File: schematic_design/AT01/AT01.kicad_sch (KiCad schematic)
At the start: 58 parts, among them J1 JST Connector, J2 Conn_01x08, J3 USB_C_Receptacle_USB2.0, J4 DC Pump Connector, J5 Solenoid Valve Connector, Q1 DMG2301L, Q2 2N7002, Q3 2N7002, SW1 SW_Push, SW2 SW_Push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

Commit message: added redesigned charging circuit
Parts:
- removed D2: LED, LED_THT:LED_D3.0mm, symbol Device:LED
- removed U4: MCP73831-2-OT, Package_TO_SOT_SMD:SOT-23-5, symbol Battery_Management:MCP73831-2-OT
- added C12, C9: 10uF, Capacitor_SMD:C_0603_1608Metric_Pad1.08x0.95mm_HandSolder, symbol Device:C
- added C15: 0.1uF, Capacitor_SMD:C_0603_1608Metric_Pad1.08x0.95mm_HandSolder, symbol Device:C_Small
- added C16: 10uF, Capacitor_SMD:C_0603_1608Metric_Pad1.08x0.95mm_HandSolder, symbol Device:C_Small
- added D10: LED, LED_THT:LED_D3.0mm, symbol Device:LED
- added D2, D9: MBRM120LT3G, Diode_SMD:D_SOD-123F, symbol Diode:MBR1020VL
- added L1: 2.7u, symbol Device:L
- added Q4: FDS6375, FDS6375:SOIC127P600X175-8N, symbol FDS6375:FDS6375
- added R18: 100m, Resistor_SMD:R_0603_1608Metric_Pad0.98x0.95mm_HandSolder, symbol Device:R
- added R19: 100K, Resistor_SMD:R_0603_1608Metric_Pad0.98x0.95mm_HandSolder, symbol Device:R
- added U4: LT1935ES5-TRPBF, S_5_ADI, symbol 2023-10-27_15-39-09:LT1935ES5-TRPBF
- added U7: MCP73844T-840I/MS, MSOP8_MC_MCH, symbol 2023-10-27_15-39-09:MCP73844T-840I_MS
- C14: footprint Capacitor_SMD:C_0402_1005Metric_Pad0.74x0.62mm_HandSolder -> CAP_FN_C_PAN; symbol Device:C_Small -> 2023-10-27_15-39-09:EEE-FN1A101UR
- C7: footprint Capacitor_SMD:C_0402_1005Metric_Pad0.74x0.62mm_HandSolder -> Capacitor_SMD:C_0603_1608Metric_Pad1.08x0.95mm_HandSolder
- J4, J5: footprint Connector_JST:JST_EH_S2B-EH_1x02_P2.50mm_Horizontal -> TerminalBlock_4Ucon:TerminalBlock_4Ucon_1x02_P3.50mm_Vertical
- R10: value 5.1K -> 10K; footprint Resistor_SMD:R_0402_1005Metric_Pad0.72x0.64mm_HandSolder -> Resistor_SMD:R_0603_1608Metric_Pad0.98x0.95mm_HandSolder
- R9: value 5.1K -> 61.2K
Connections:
- net GND: now also C14.1, C7.2, R10.2, C12.2, C15.2, C16.2, C9.2, U4.2 (GND), U7.6 (VSS); no longer C14.2, C7.1, R9.2
- net VBAT: now also C14.2, C16.1, Q4.5, U7.7 (VBAT); no longer C14.1, C7.2
- net VBUS: now also C7.1, L1.1, U4.4 (*SHDN), U4.5 (VIN)
- net at R10.1: now also R9.2, U4.3 (FB)
- net at R9.1: now also C9.1, D2.1 (K), D9.2 (A)
- new net: C15.1, U7.5 (TIMER)
- new net: Q4.1, R18.2, U7.1 (SENSE)
- new net: Q4.4, U7.8 (DRV)
- new net: C12.1, D10.2 (A), D9.1 (K), R18.1, R19.1, U7.2 (VDD)
- new net: D10.1 (K), U7.3 (STAT1)
- new net: R19.2, U7.4 (EN)
- new net: D2.2 (A), L1.2, U4.1 (SW)
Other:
- added sheet AT01_Lipo (AT01_Lipo.kicad_sch)
- note added: "9V"
- moved on the sheet: C10, C13, C8, D1, H1, H2, H3, H4, J1, Q1, R3, U6

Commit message: updated FTDI board
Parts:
- removed J2: Conn_01x08, Connector_PinHeader_1.00mm:PinHeader_1x08_P1.00mm_Vertical, symbol Connector_Generic:Conn_01x08
- added C17: 0.1uF, Capacitor_SMD:C_0402_1005Metric_Pad0.74x0.62mm_HandSolder, symbol Device:C
- added C18: 10uF, Capacitor_SMD:C_0402_1005Metric_Pad0.74x0.62mm_HandSolder, symbol Device:C_Small
- added J2: Conn_01x07, Connector_PinHeader_1.00mm:PinHeader_1x07_P1.00mm_Vertical, symbol Connector_Generic:Conn_01x07
- added R20: 5.1K, Resistor_SMD:R_0402_1005Metric_Pad0.72x0.64mm_HandSolder, symbol Device:R
- C12, C15, C16, C7, C9: footprint Capacitor_SMD:C_0603_1608Metric_Pad1.08x0.95mm_HandSolder -> Capacitor_SMD:C_0402_1005Metric_Pad0.74x0.62mm_HandSolder
- J4, J5: footprint TerminalBlock_4Ucon:TerminalBlock_4Ucon_1x02_P3.50mm_Vertical -> TerminalBlock_4Ucon:TerminalBlock_4Ucon_1x02_P3.50mm_Horizontal
- L1: footprint (none) -> Library:IND_R2NC_SUM
- Q4: footprint FDS6375:SOIC127P600X175-8N -> Library:SOIC127P600X175-8N
- R10, R18, R19: footprint Resistor_SMD:R_0603_1608Metric_Pad0.98x0.95mm_HandSolder -> Capacitor_SMD:C_0402_1005Metric_Pad0.74x0.62mm_HandSolder
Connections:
- net BL_SCREEN is gone; now on net SDA: U5.7 (IO35)
- net 3V3: now also C17.1, J2.1 (Pin_1), R20.1
- net CS: now also U5.14 (IO12), J2.6 (Pin_6); no longer U5.8 (IO32)
- net DC_SCREEN: now also U5.10 (IO25), J2.3 (Pin_3); no longer U5.9 (IO33)
- net DRV_FAULT: now also U5.26 (IO4); no longer U5.12 (IO27)
- net DRV_SLEEP: now also U5.27 (IO16); no longer U5.11 (IO26)
- net GND: now also C17.2, C18.2, J2.2 (Pin_2)
- net GPIO0: now also R20.2
- net MOSI: now also U5.16 (IO13), J2.7 (Pin_7); no longer U5.30 (IO18)
- net MOTOR_PIN_1: now also U5.30 (IO18); no longer U5.14 (IO12)
- net MOTOR_PIN_2: now also U5.31 (IO19); no longer U5.16 (IO13)
- net RST_SCREEN: now also U5.11 (IO26), J2.4 (Pin_4); no longer U5.6 (IO34)
- net SCK: now also U5.13 (IO14), J2.5 (Pin_5); no longer U5.29 (IO5)
- net SCL: now also U5.6 (IO34); no longer U5.36 (IO22)
- net SDA: no longer U5.37 (IO23)
- net SOLENOID_PIN_1: now also U5.28 (IO17); no longer U5.13 (IO14)
- net SOLENOID_PIN_2: now also U5.29 (IO5); no longer U5.23 (IO15)
- net VBAT: now also Q1.2 (S); no longer Q1.3 (D)
- net at R17.2, SW3.2: now also U5.36 (IO22); no longer U5.10 (IO25)
- net at R15.2: now also U5.23 (IO15); no longer U5.27 (IO16)
- net at R16.2, SW2.2: now also U5.37 (IO23); no longer U5.33 (IO21)
- net at R11.2, R8.1, U5.4 (SENSOR_VP): now also C18.1
- net at C8.1, D1.1 (K), U6.3 (VI): now also Q1.3 (D); no longer Q1.2 (S)
- no-connect marks 28 -> 29
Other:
- moved on the sheet: C10

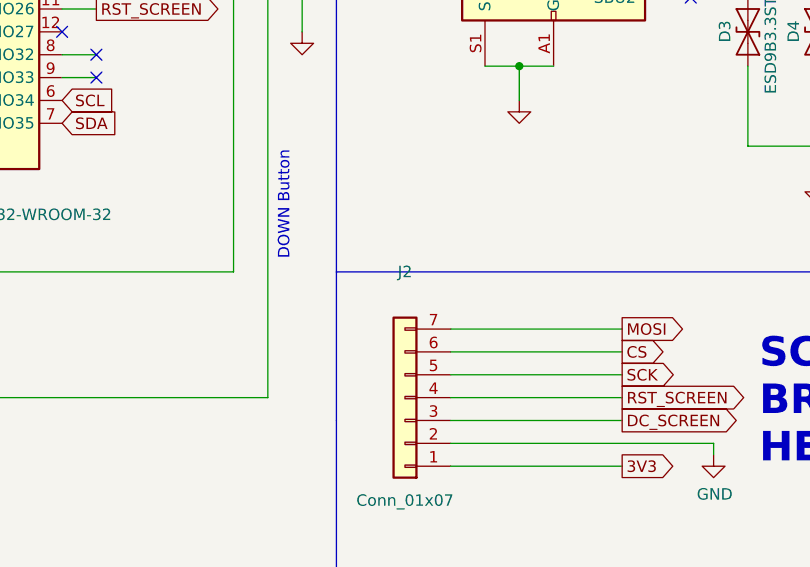
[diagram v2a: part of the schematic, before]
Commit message: adding design recommendations from call with Yi
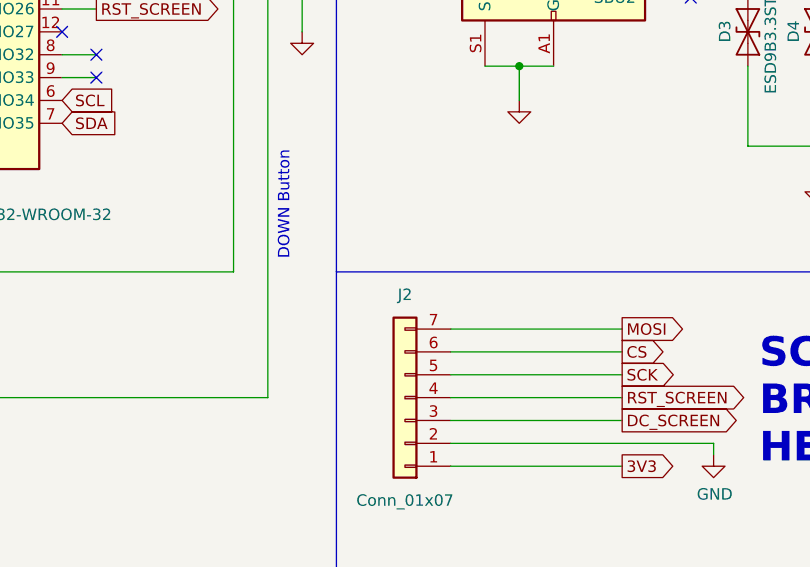
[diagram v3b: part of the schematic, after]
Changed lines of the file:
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@@
   (symbol (lib_id "Connector_Generic:Conn_01x07") (at 109.22 180.34 180) (unit 1)
     (in_bom yes) (on_board yes) (dnp no)
-    (property "Reference" "J2" (at 109.22 166.37 0)
+    (property "Reference" "J2" (at 109.22 168.91 0)
       (effects (font (size 1.27 1.27)))
     )
